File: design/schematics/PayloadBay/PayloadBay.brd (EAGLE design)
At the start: 100 x 80 mm, 25 parts, among them IC1 MC33269ST-5.0T3, IC2 MC33269D-5.0, IC3 ATMEGA2560-16AU, Q2 16MHz, X1 DC21MMX, Y1 16MHz

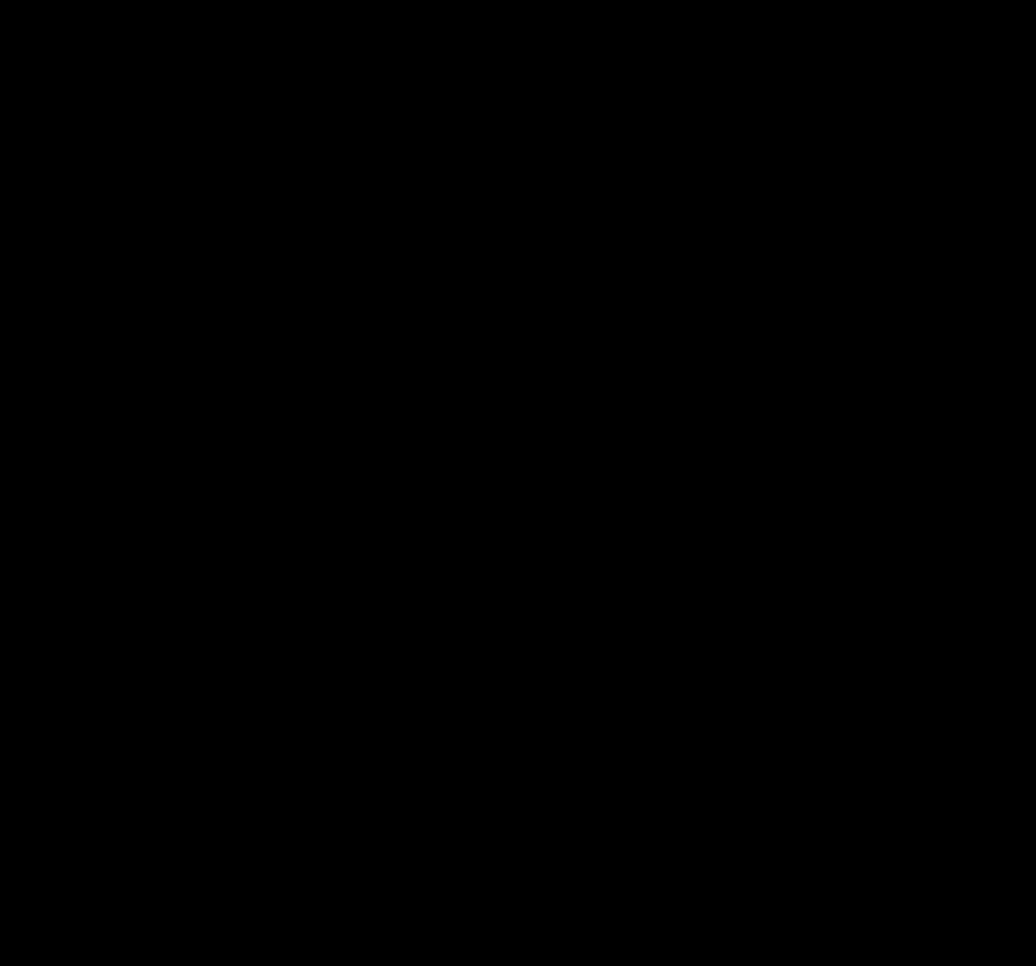
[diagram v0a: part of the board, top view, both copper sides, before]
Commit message: Updated payload bay schematic
* added text, reed switch, limit switches, mosfet, and motor
* added png version of schematic
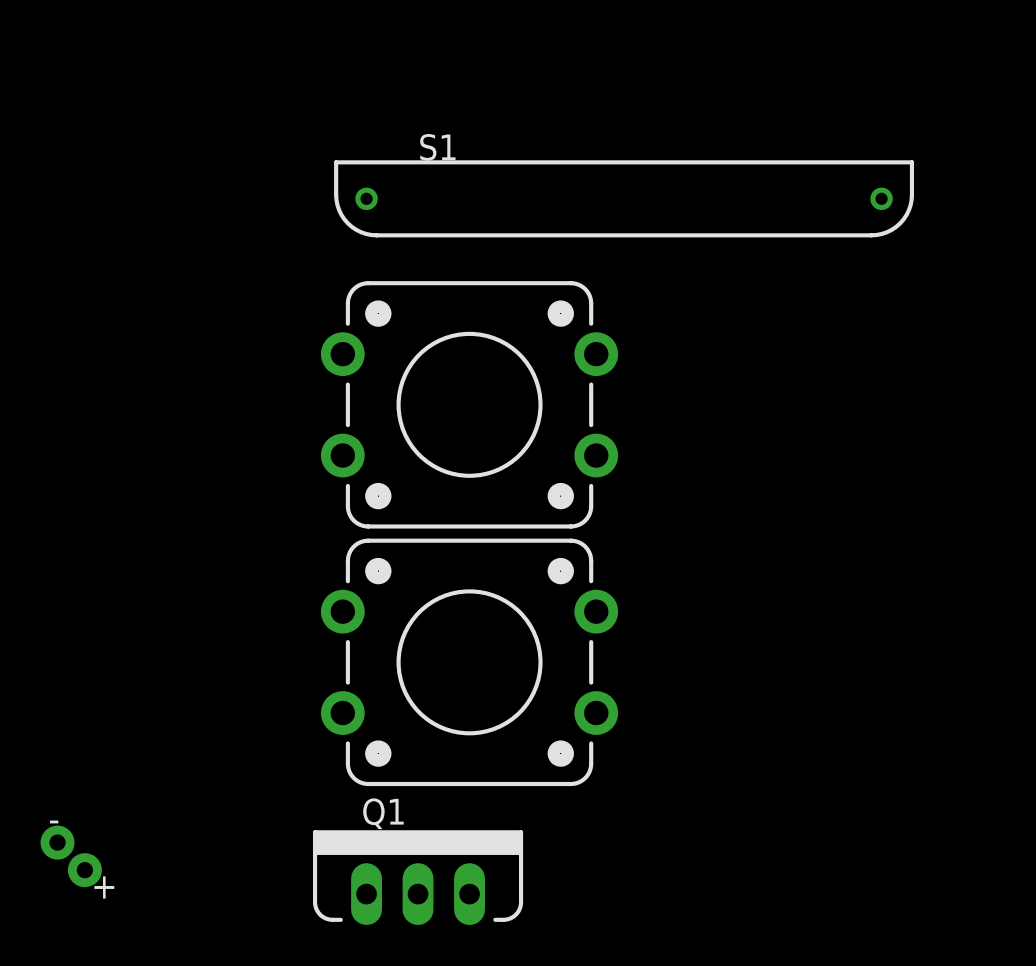
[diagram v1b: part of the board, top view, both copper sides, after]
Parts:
- added LIMIT-CLOSED, LIMIT-OPEN: 2 Terminal Limit Switch, SparkFun-Electromechanical:TACTILE-PTH-12MM
- added PAYLOAD-BAY-MOTOR: MOTOR10MM, SparkFun-Electromechanical:VIBE-MOTOR-10MM
- added Q1: MOSFET-PCHANNELFQP27P06, SparkFun-DiscreteSemi:TO220V
- added S1: REED-SWITCH-MK6-10, switch-reed:MK6-10
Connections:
- new net N$1: PAYLOAD-BAY-MOTOR.+, Q1.3
- new net PE6: IC3.8, LIMIT-CLOSED.3, RN3.7
- new net PE7: IC3.9, RN1.5, S1.2
- net +5V: now also LIMIT-CLOSED.1, LIMIT-OPEN.1, Q1.2, S1.1
- net GND: now also PAYLOAD-BAY-MOTOR.-, RN1.4, RN3.1, RN3.2
- net PC0: now also Q1.1
- net PE5: now also LIMIT-OPEN.3, RN3.8

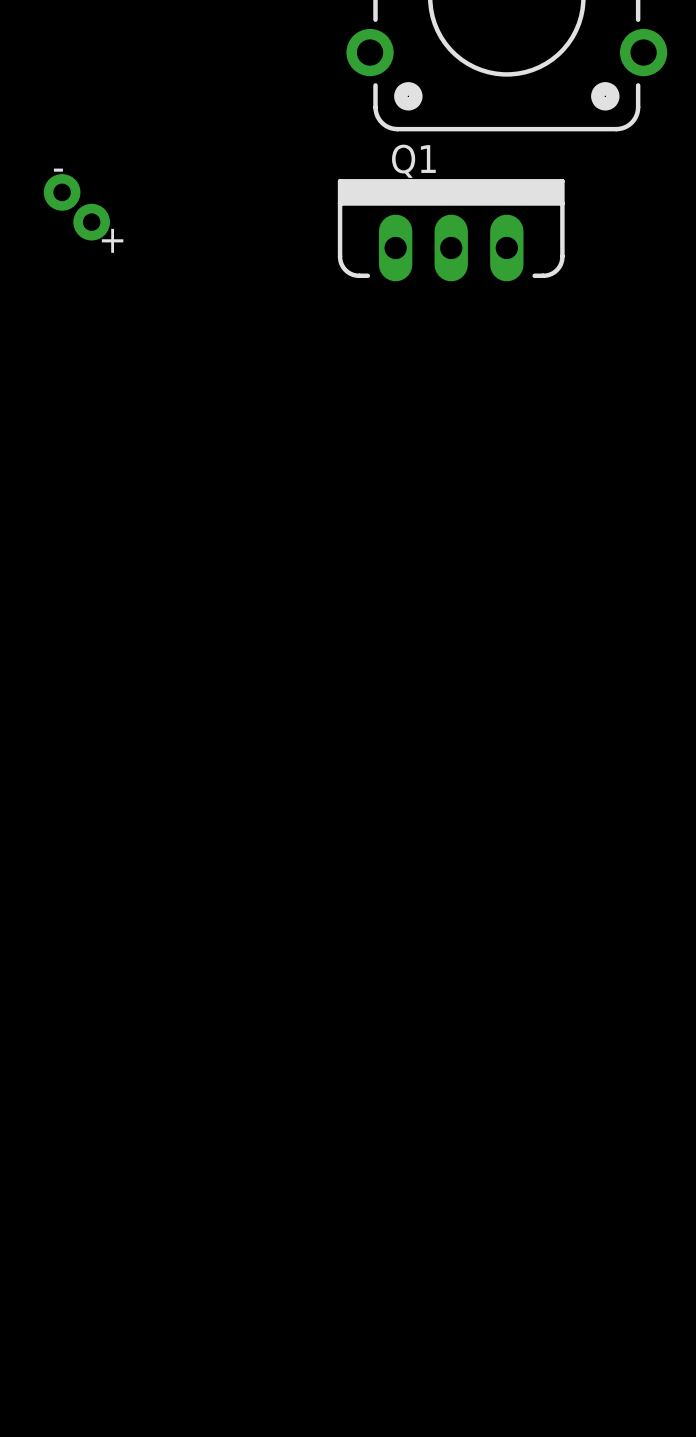
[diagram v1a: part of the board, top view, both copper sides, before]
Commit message: fixed lack of motor control
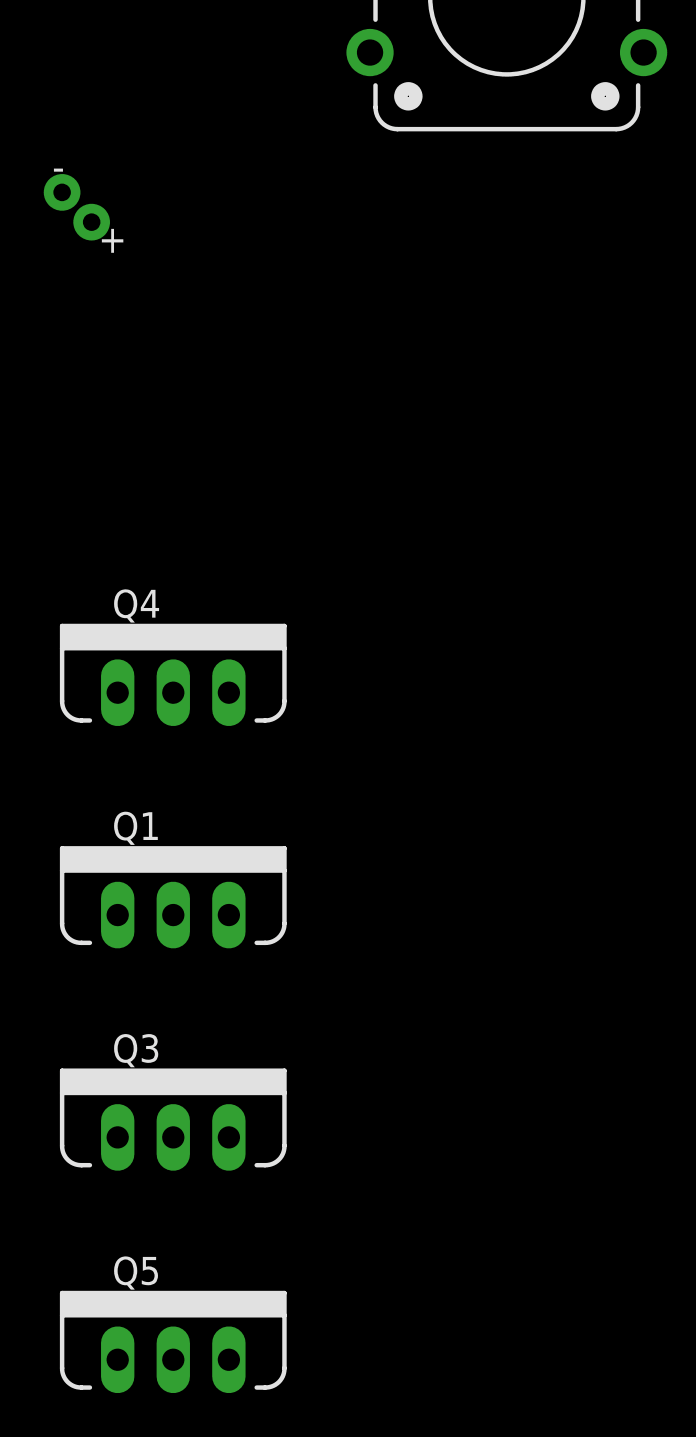
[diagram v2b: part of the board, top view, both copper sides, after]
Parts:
- added Q3, Q5: NFET-FQP30N06L, SparkFun-DiscreteSemi:TO220V
- added Q4: PFET-FQP27P06, SparkFun-DiscreteSemi:TO220V
- Q1: value MOSFET-PCHANNELFQP27P06 -> PFET-FQP27P06
- moved Q1 33.0 mm to (-68.6, -74.9)
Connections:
- new net N$4: PAYLOAD-BAY-MOTOR.-, Q3.2, Q4.3
- net +5V: now also Q4.2
- net GND: now also Q3.3, Q5.3; no longer PAYLOAD-BAY-MOTOR.-
- net N$1: now also Q5.2
- net PC0: no longer Q1.1
- net PC1: now also Q3.1
- net PC2: now also Q5.1
- net PC3: now also Q4.1
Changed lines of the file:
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@@
 <attribute name="PROD_ID" value="SWCH-09185" x="-53.34" y="-33.02" size="1.778" layer="27" display="off"/>
 </element>
-<element name="Q1" library="SparkFun-DiscreteSemi" package="TO220V" value="MOSFET-PCHANNELFQP27P06" x="-55.88" y="-44.45"/>
 <element name="PAYLOAD-BAY-MOTOR" library="SparkFun-Electromechanical" package="VIBE-MOTOR-10MM" value="MOTOR10MM" x="-67.31" y="-39.37"/>
+<element name="Q4" library="SparkFun-DiscreteSemi" package="TO220V" value="PFET-FQP27P06" x="-68.58" y="-64.77"/>
+<element name="Q1" library="SparkFun-DiscreteSemi" package="TO220V" value="PFET-FQP27P06" x="-68.58" y="-74.93"/>
+<element name="Q3" library="SparkFun-DiscreteSemi" package="TO220V" value="NFET-FQP30N06L" x="-68.58" y="-85.09">
+<attribute name="PROD_ID" value="TRANS-10060" x="-68.58" y="-85.09" size="1.778" layer="27" display="off"/>
+</element>
+<element name="Q5" library="SparkFun-DiscreteSemi" package="TO220V" value="NFET-FQP30N06L" x="-68.58" y="-95.25">
+<attribute name="PROD_ID" value="TRANS-10060" x="-68.58" y="-95.25" size="1.778" layer="27" display="off"/>
+</element>
 </elements>
 <signals>
@@
 <contactref element="S1" pad="1"/>
 <contactref element="Q1" pad="2"/>
-<wire x1="-47.09" y1="-35.52" x2="-55.88" y2="-44.45" width="0" layer="19" extent="1-1"/>
+<contactref element="Q4" pad="2"/>
+<wire x1="-68.58" y1="-64.77" x2="-68.58" y2="-74.93" width="0" layer="19" extent="1-1"/>
+<wire x1="-47.09" y1="-35.52" x2="-68.58" y2="-64.77" width="0" layer="19" extent="1-1"/>
 <wire x1="-47.09" y1="-22.82" x2="-47.09" y2="-35.52" width="0" layer="19" extent="1-1"/>
 <wire x1="-58.42" y1="-10.16" x2="-47.09" y2="-22.82" width="0" layer="19" extent="1-1"/>
@@
 <contactref element="RN3" pad="1"/>
 <contactref element="RN1" pad="4"/>
-<contactref element="PAYLOAD-BAY-MOTOR" pad="-"/>
-<wire x1="-45.46" y1="1.55" x2="-73.66" y2="-41.91" width="0" layer="19" extent="1-1"/>
+<contactref element="Q5" pad="3"/>
+<contactref element="Q3" pad="3"/>
+<wire x1="-66.04" y1="-85.09" x2="-66.04" y2="-95.25" width="0" layer="19" extent="1-1"/>
+<wire x1="-45.46" y1="1.55" x2="-66.04" y2="-85.09" width="0" layer="19" extent="1-1"/>
 <wire x1="-35.94" y1="9.89" x2="-45.46" y2="1.55" width="0" layer="19" extent="1-1"/>
 <wire x1="-33.44" y1="16.89" x2="-35.94" y2="9.89" width="0" layer="19" extent="1-1"/>
@@
 <signal name="PC0">
 <contactref element="IC3" pad="53"/>
-<contactref element="Q1" pad="1"/>
-<wire x1="-19.94" y1="3.89" x2="-58.42" y2="-44.45" width="0" layer="19" extent="1-1"/>
 </signal>
 <signal name="PC1">
 <contactref element="IC3" pad="54"/>
+<contactref element="Q3" pad="1"/>
+<wire x1="-19.94" y1="4.39" x2="-71.12" y2="-85.09" width="0" layer="19" extent="1-1"/>
 </signal>
 <signal name="PC2">
 <contactref element="IC3" pad="55"/>
+<contactref element="Q5" pad="1"/>
+<wire x1="-19.94" y1="4.89" x2="-71.12" y2="-95.25" width="0" layer="19" extent="1-1"/>
 </signal>
 <signal name="PC3">
 <contactref element="IC3" pad="56"/>
+<contactref element="Q4" pad="1"/>
+<wire x1="-19.94" y1="5.39" x2="-71.12" y2="-64.77" width="0" layer="19" extent="1-1"/>
 </signal>
 <signal name="PC4">
@@
 </signal>
 <signal name="N$1">
+<contactref element="Q1" pad="3"/>
 <contactref element="PAYLOAD-BAY-MOTOR" pad="+"/>
-<contactref element="Q1" pad="3"/>
-<wire x1="-53.34" y1="-44.45" x2="-72.31" y2="-43.27" width="0" layer="19" extent="1-1"/>
+<contactref element="Q5" pad="2"/>
+<wire x1="-66.04" y1="-74.93" x2="-68.58" y2="-95.25" width="0" layer="19" extent="1-1"/>
+<wire x1="-72.31" y1="-43.27" x2="-66.04" y2="-74.93" width="0" layer="19" extent="1-1"/>
+</signal>
+<signal name="N$4">
+<contactref element="Q3" pad="2"/>
+<contactref element="PAYLOAD-BAY-MOTOR" pad="-"/>
+<contactref element="Q4" pad="3"/>
+<wire x1="-66.04" y1="-64.77" x2="-68.58" y2="-85.09" width="0" layer="19" extent="1-1"/>
+<wire x1="-73.66" y1="-41.91" x2="-66.04" y2="-64.77" width="0" layer="19" extent="1-1"/>
 </signal>
 </signals>
